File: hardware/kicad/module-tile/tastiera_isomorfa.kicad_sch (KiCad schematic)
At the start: 4 parts, among them J1 Conn_LEFT, J2 Conn_TOP, J3 Conn_BOTTOM, J4 Conn_RIGHT

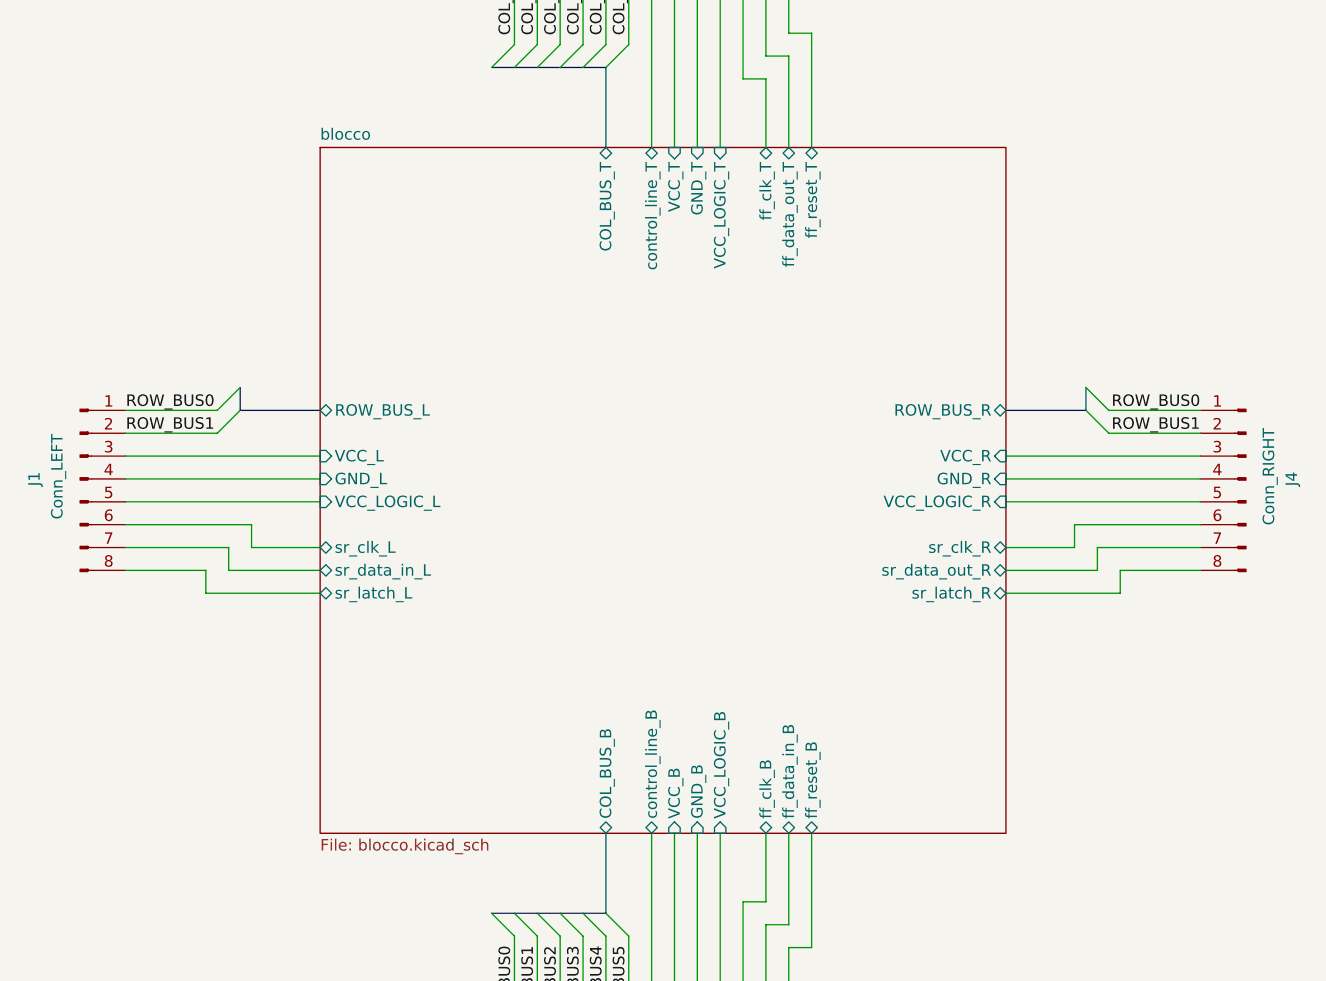
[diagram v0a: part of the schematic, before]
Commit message: Added horizontal control line UTF-8 like. Updated capacitor and resistor values.
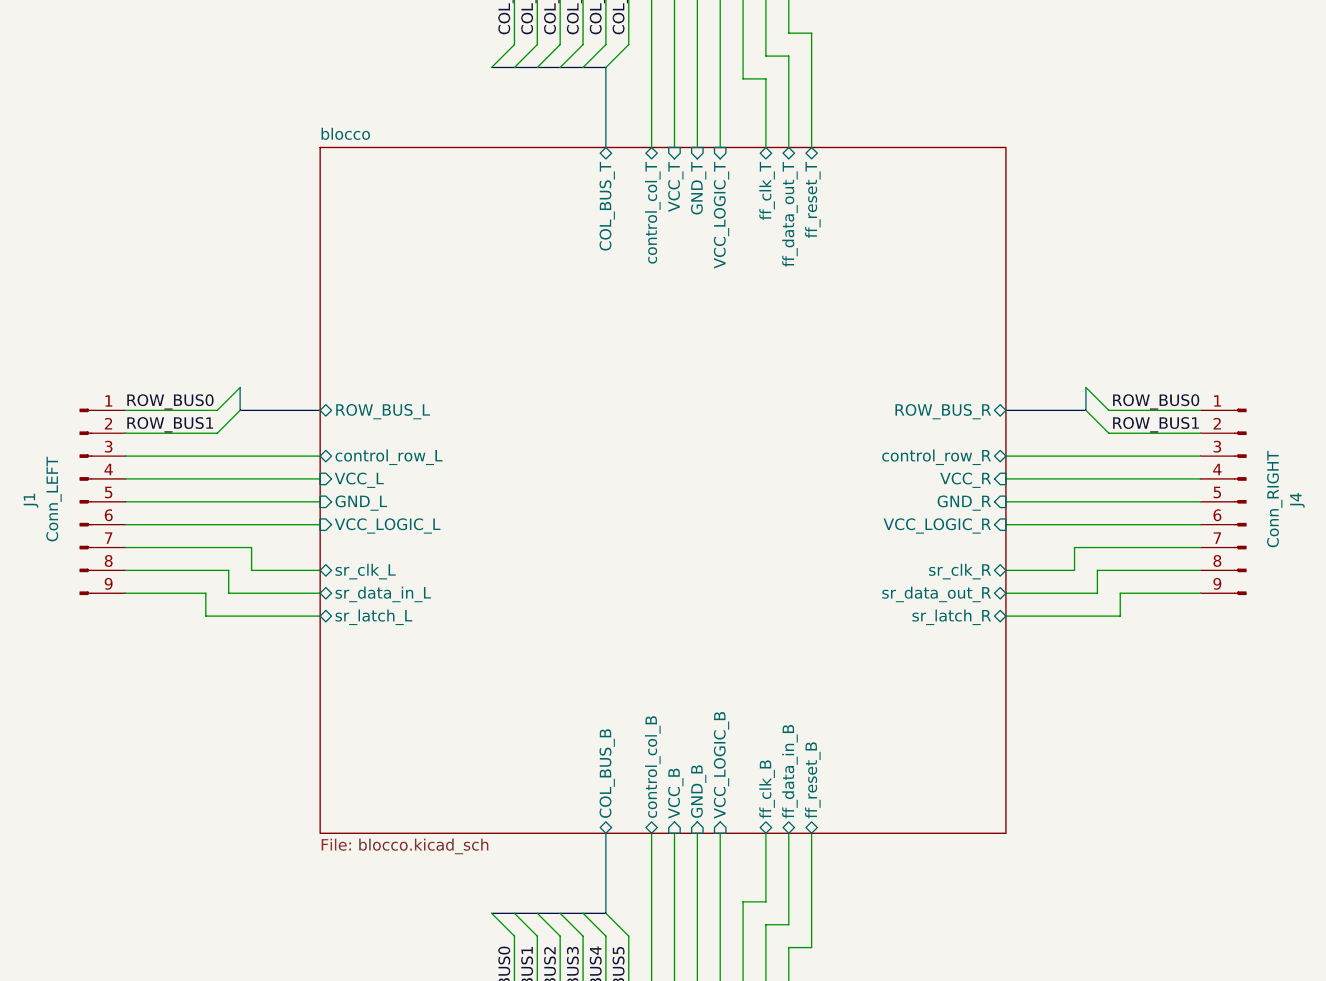
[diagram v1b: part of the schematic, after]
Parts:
- removed J1: Conn_LEFT, symbol Connector:Conn_01x08_Pin
- removed J4: Conn_RIGHT, symbol Connector:Conn_01x08_Pin
- added J1: Conn_LEFT, symbol Connector:Conn_01x09_Pin
- added J4: Conn_RIGHT, symbol Connector:Conn_01x09_Pin
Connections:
- net ROW_BUS0: now also J1.1 (Pin_1), J4.1 (Pin_1)
- net ROW_BUS1: now also J1.2 (Pin_2), J4.2 (Pin_2)
- net blocco/GND_L: now also J1.5 (Pin_5)
- net blocco/GND_R: now also J4.5 (Pin_5)
- net blocco/VCC_L: now also J1.4 (Pin_4)
- net blocco/VCC_LOGIC_L: now also J1.6 (Pin_6)
- net blocco/VCC_LOGIC_R: now also J4.6 (Pin_6)
- net blocco/VCC_R: now also J4.4 (Pin_4)
- net blocco/sr_clk_L: now also J1.7 (Pin_7)
- net blocco/sr_clk_R: now also J4.7 (Pin_7)
- net blocco/sr_data_in_L: now also J1.8 (Pin_8)
- net blocco/sr_data_out_R: now also J4.8 (Pin_8)
- net blocco/sr_latch_L: now also J1.9 (Pin_9)
- net blocco/sr_latch_R: now also J4.9 (Pin_9)
- net blocco/control_line_B renamed blocco/control_col_B
- net blocco/control_line_T renamed blocco/control_col_T
- new net blocco/control_row_L: J1.3 (Pin_3)
- new net blocco/control_row_R: J4.3 (Pin_3)
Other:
- sheet blocco ports: added control_col_B, control_col_T, control_row_L, control_row_R; removed control_line_B, control_line_T

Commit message: starting new topology
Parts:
- removed J1: Conn_LEFT, symbol Connector:Conn_01x09_Pin
- removed J2: Conn_TOP, symbol Connector:Conn_01x13_Pin
- removed J3: Conn_BOTTOM, symbol Connector:Conn_01x13_Pin
- removed J4: Conn_RIGHT, symbol Connector:Conn_01x09_Pin
- added SW1, SW10, SW11, SW12, SW2, SW3, SW4, SW5, SW6, SW7, SW8, SW9: ~, symbol Switch:SW_Push_45deg
- added U1, U2: 74HC165, symbol 74xx:74HC165
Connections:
- new net: SW1.1, SW10.1, SW11.1, SW12.1, SW2.1, SW3.1, SW4.1, SW5.1, SW6.1, SW7.1, SW8.1, SW9.1
- new net: SW12.2, U1.6 (D7)
- new net: SW8.2, U1.14 (D3)
- new net: U1.10 (DS), U2.9 (Q7)
- new net: SW5.2, U1.11 (D0)
- new net: SW6.2, U1.12 (D1)
- new net: SW7.2, U1.13 (D2)
- new net: SW9.2, U1.3 (D4)
- new net: SW10.2, U1.4 (D5)
- new net: SW11.2, U1.5 (D6)
- new net: SW4.2, U2.6 (D7)
- new net: SW2.2, U2.4 (D5)
- new net: SW1.2, U2.3 (D4)
- new net: SW3.2, U2.5 (D6)
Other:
- removed sheet blocco

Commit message: Init VHDL simulation
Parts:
- added R1, R2, R3: R, symbol Device:R
- added U3, U4: 74AHCT125, symbol 74xx:74AHCT125
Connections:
- net at SW1.1, SW10.1, SW11.1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: now also R3.1
- net at U2.10 (DS): now also U3.8, U4.8
- net at U2.11 (D0): now also R2.2
- net at U2.12 (D1): now also R1.2
- new net: U3.5, U4.5
- new net: U3.2, U4.2
- new net VCC: R1.1, R2.1, R3.2

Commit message: Start kicad design
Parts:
- removed R1, R2, R3: R, symbol Device:R
- removed SW1, SW10, SW11, SW12, SW2, SW3, SW4, SW5, SW6, SW7, SW8, SW9: ~, symbol Switch:SW_Push_45deg
- removed U3, U4: 74AHCT125, symbol 74xx:74AHCT125
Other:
- added sheet keyboard (keyboard.kicad_sch)

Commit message: Improving schematics
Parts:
- added U4: 74AUC2G08, symbol 74xGxx:74AUC2G08
- added U5: 74LS73, symbol 74xx:74LS73
- added U6: 74AUC2G125, symbol 74xGxx:74AUC2G125
- added U7: 74AUC2G126, symbol 74xGxx:74AUC2G126
- added U8: 74AHC1G32, symbol 74xGxx:74AHC1G32
- added U9: 74AHC1G04, symbol 74xGxx:74AHC1G04
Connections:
- net counter/~{rst}: now reaches U1.1 (~{PL})
- net counter/~{rst}: now also U2.1 (~{PL}), U9.4
- net BTNs7: now reaches U1.11 (D0)
- net BTNs6: now reaches U1.12 (D1)
- net BTNs5: now reaches U1.13 (D2)
- net BTNs4: now reaches U1.14 (D3)
- net GND: now reaches U1.15 (~{CE})
- net GND: now also U1.8 (GND), U2.15 (~{CE}), U2.8 (GND), U8.3 (GND), U9.3 (GND)
- net VCC: now reaches U1.16 (VCC)
- net VCC: now also U2.13 (D2), U2.14 (D3), U2.16 (VCC), U8.5 (VCC), U9.5 (VCC)
- net B_clk: now reaches U1.2 (CP)
- net B_clk: now also U2.2 (CP), U6.2, U7.2
- net BTNs3: now reaches U1.3 (D4)
- net BTNs2: now reaches U1.4 (D5)
- net BTNs1: now reaches U1.5 (D6)
- net BTNs0: now reaches U1.6 (D7)
- net B_data: now reaches U1.9 (Q7)
- net at U2.10 (DS): now also U6.3, U7.3
- net T_endcol: now reaches U2.11 (D0)
- net L_endrow: now reaches U2.12 (D1)
- net BTNs11: now reaches U2.3 (D4)
- net BTNs10: now reaches U2.4 (D5)
- net BTNs9: now reaches U2.5 (D6)
- net BTNs8: now reaches U2.6 (D7)
- new net: U4.3, U6.1, U6.7, U7.1, U7.7
- new net B_first: U4.6
- new net B_latch: U8.1
- new net L_clk: U7.6
- new net L_data: U7.5
- new net L_latch: U8.4, U9.2
- new net R_latch: U8.2
- new net T_W: U4.5
- new net T_clk: U6.6
- no-connect marks 0 -> 2
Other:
- added sheet counter (counter.kicad_sch)
- sheet keyboard ports: added BTNs; removed none
- moved on the sheet: U1, U2

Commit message: Schematics update
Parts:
- removed U1, U2: 74HC165, symbol 74xx:74HC165
- removed U4: 74AUC2G08, symbol 74xGxx:74AUC2G08
- removed U5: 74LS73, symbol 74xx:74LS73
- removed U6: 74AUC2G125, symbol 74xGxx:74AUC2G125
- removed U7: 74AUC2G126, symbol 74xGxx:74AUC2G126
- removed U8: 74AHC1G32, symbol 74xGxx:74AHC1G32
- removed U9: 74AHC1G04, symbol 74xGxx:74AHC1G04
- added J1, J2: Conn_01x08, symbol Connector_Generic:Conn_01x08
- added J3, J4: Conn_01x06, symbol Connector_Generic:Conn_01x06
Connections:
- net GND: now also J1.8 (Pin_8), J2.8 (Pin_8), J3.6 (Pin_6), J4.6 (Pin_6)
- net VCC: now also J1.1 (Pin_1), J2.1 (Pin_1), J3.1 (Pin_1), J4.1 (Pin_1)
- new net tile/B_W: J1.7 (Pin_7)
- new net tile/B_clk: J1.2 (Pin_2)
- new net tile/B_data: J1.3 (Pin_3)
- new net tile/B_endcol: J1.4 (Pin_4)
- new net tile/B_first: J1.5 (Pin_5)
- new net tile/B_latch: J1.6 (Pin_6)
- new net tile/L_clk: J3.2 (Pin_2)
- new net tile/L_data: J3.3 (Pin_3)
- new net tile/L_endrow: J3.4 (Pin_4)
- new net tile/L_latch: J3.5 (Pin_5)
- new net tile/R_clk: J4.2 (Pin_2)
- new net tile/R_data: J4.3 (Pin_3)
- new net tile/R_endrow: J4.4 (Pin_4)
- new net tile/R_latch: J4.5 (Pin_5)
- new net tile/T_W: J2.7 (Pin_7)
- new net tile/T_clk: J2.2 (Pin_2)
- new net tile/T_data: J2.3 (Pin_3)
- new net tile/T_endcol: J2.4 (Pin_4)
- new net tile/T_first: J2.5 (Pin_5)
- new net tile/T_latch: J2.6 (Pin_6)
- no-connect marks 2 -> 0
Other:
- removed sheet counter
- removed sheet keyboard
- added sheet tile (tile.kicad_sch)

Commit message: Schematic complete
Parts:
- J101: renamed from J3; value Conn_01x06 -> Conn_LEFT; footprint (none) -> Connector_PinHeader_2.54mm:PinHeader_1x06_P2.54mm_Vertical
- J102: renamed from J2; value Conn_01x08 -> Conn_TOP; footprint (none) -> Connector_PinHeader_2.54mm:PinHeader_1x08_P2.54mm_Vertical
- J103: renamed from J1; value Conn_01x08 -> Conn_BOTTOM; footprint (none) -> Connector_PinHeader_2.54mm:PinHeader_1x08_P2.54mm_Vertical
- J104: renamed from J4; value Conn_01x06 -> Conn_RIGHT; footprint (none) -> Connector_PinHeader_2.54mm:PinHeader_1x06_P2.54mm_Vertical
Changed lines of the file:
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@@
 		(on_board yes)
 		(dnp no)
-		(property "Reference" "J2"
+		(property "Reference" "J102"
 			(at 152.4 40.64 90)
 			(effects
@@
 			)
 		)
-		(property "Value" "Conn_01x08"
+		(property "Value" "Conn_TOP"
 			(at 152.4 38.1 90)
 			(effects
@@
 			)
 		)
-		(property "Footprint" ""
+		(property "Footprint" "Connector_PinHeader_2.54mm:PinHeader_1x08_P2.54mm_Vertical"
 			(at 151.13 44.45 0)
 			(effects
@@
 			)
 		)
+		(property "Codice" ""
+			(at 151.13 44.45 90)
+			(effects
+				(font
+					(size 1.27 1.27)
+				)
+				(hide yes)
+			)
+		)
+		(property "Link" ""
+			(at 151.13 44.45 90)
+			(effects
+				(font
+					(size 1.27 1.27)
+				)
+				(hide yes)
+			)
+		)
 		(pin "7"
 		)
@@
 			(project "tastiera_isomorfa"
 				(path "/2a6329ec-b0e8-4012-8f5a-476608b8b2cc"
-					(reference "J2")
+					(reference "J102")
 					(unit 1)
 				)
@@
 		(dnp no)
 		(fields_autoplaced yes)
-		(property "Reference" "#PWR029"
+		(property "Reference" "#PWR0103"
 			(at 137.16 53.34 0)
 			(effects
@@
 			(project ""
 				(path "/2a6329ec-b0e8-4012-8f5a-476608b8b2cc"
-					(reference "#PWR029")
+					(reference "#PWR0103")
 					(unit 1)
 				)
@@
 		(dnp no)
 		(fields_autoplaced yes)
-		(property "Reference" "J3"
+		(property "Reference" "J101"
 			(at 100.33 83.82 0)
 			(effects
@@
 			)
 		)
-		(property "Value" "Conn_01x06"
+		(property "Value" "Conn_LEFT"
 			(at 100.33 86.36 0)
 			(effects
@@
 			)
 		)
-		(property "Footprint" ""
+		(property "Footprint" "Connector_PinHeader_2.54mm:PinHeader_1x06_P2.54mm_Vertical"
 			(at 100.33 95.25 0)
 			(effects
@@
 			)
 		)
+		(property "Codice" ""
+			(at 100.33 95.25 0)
+			(effects
+				(font
+					(size 1.27 1.27)
+				)
+				(hide yes)
+			)
+		)
+		(property "Link" ""
+			(at 100.33 95.25 0)
+			(effects
+				(font
+					(size 1.27 1.27)
+				)
+				(hide yes)
+			)
+		)
 		(pin "1"
 		)
@@
 			(project ""
 				(path "/2a6329ec-b0e8-4012-8f5a-476608b8b2cc"
-					(reference "J3")
+					(reference "J101")
 					(unit 1)
 				)
@@
 		(dnp no)
 		(fields_autoplaced yes)
-		(property "Reference" "#PWR036"
+		(property "Reference" "#PWR0102"
 			(at 109.22 113.03 0)
 			(effects
@@
 			(project ""
 				(path "/2a6329ec-b0e8-4012-8f5a-476608b8b2cc"
-					(reference "#PWR036")
+					(reference "#PWR0102")
 					(unit 1)
 				)
@@
 		(dnp no)
 		(fields_autoplaced yes)
-		(property "Reference" "#PWR035"
+		(property "Reference" "#PWR0108"
 			(at 195.58 113.03 0)
 			(effects
@@
 			(project ""
 				(path "/2a6329ec-b0e8-4012-8f5a-476608b8b2cc"
-					(reference "#PWR035")
+					(reference "#PWR0108")
 					(unit 1)
 				)
@@
 		(dnp no)
 		(fields_autoplaced yes)
-		(property "Reference" "#PWR034"
+		(property "Reference" "#PWR0106"
 			(at 167.64 149.86 0)
 			(effects
@@
 			(project ""
 				(path "/2a6329ec-b0e8-4012-8f5a-476608b8b2cc"
-					(reference "#PWR034")
+					(reference "#PWR0106")
 					(unit 1)
 				)
@@
 		(dnp no)
 		(fields_autoplaced yes)
-		(property "Reference" "#PWR030"
+		(property "Reference" "#PWR0104"
 			(at 143.51 147.32 0)
 			(effects
@@
 			(project ""
 				(path "/2a6329ec-b0e8-4012-8f5a-476608b8b2cc"
-					(reference "#PWR030")
+					(reference "#PWR0104")
 					(unit 1)
 				)
@@
 		(dnp no)
 		(fields_autoplaced yes)
-		(property "Reference" "#PWR031"
+		(property "Reference" "#PWR0107"
 			(at 195.58 91.44 0)
 			(effects
@@
 			(project ""
 				(path "/2a6329ec-b0e8-4012-8f5a-476608b8b2cc"
-					(reference "#PWR031")
+					(reference "#PWR0107")
 					(unit 1)
 				)
@@
 		(dnp no)
 		(fields_autoplaced yes)
-		(property "Reference" "#PWR033"
+		(property "Reference" "#PWR0105"
 			(at 161.29 55.88 0)
 			(effects
@@
 			(project ""
 				(path "/2a6329ec-b0e8-4012-8f5a-476608b8b2cc"
-					(reference "#PWR033")
+					(reference "#PWR0105")
 					(unit 1)
 				)
@@
 		(dnp no)
 		(fields_autoplaced yes)
-		(property "Reference" "#PWR032"
+		(property "Reference" "#PWR0101"
 			(at 109.22 91.44 0)
 			(effects
@@
 			(project ""
 				(path "/2a6329ec-b0e8-4012-8f5a-476608b8b2cc"
-					(reference "#PWR032")
+					(reference "#PWR0101")
 					(unit 1)
 				)
@@
 		(dnp no)
 		(fields_autoplaced yes)
-		(property "Reference" "J4"
-			(at 204.47 83.82 0)
-			(effects
-				(font
-					(size 1.27 1.27)
-				)
-			)
-		)
-		(property "Value" "Conn_01x06"
-			(at 204.47 86.36 0)
-			(effects
-				(font
-					(size 1.27 1.27)
-				)
-			)
-		)
-		(property "Footprint" ""
+		(property "Reference" "J104"
+			(at 207.01 95.2499 0)
+			(effects
+				(font
+					(size 1.27 1.27)
+				)
+				(justify left)
+			)
+		)
+		(property "Value" "Conn_RIGHT"
+			(at 207.01 97.7899 0)
+			(effects
+				(font
+					(size 1.27 1.27)
+				)
+				(justify left)
+			)
+		)
+		(property "Footprint" "Connector_PinHeader_2.54mm:PinHeader_1x06_P2.54mm_Vertical"
 			(at 204.47 95.25 0)
 			(effects
@@
 			)
 		)
+		(property "Codice" ""
+			(at 204.47 95.25 0)
+			(effects
+				(font
+					(size 1.27 1.27)
+				)
+				(hide yes)
+			)
+		)
+		(property "Link" ""
+			(at 204.47 95.25 0)
+			(effects
+				(font
+					(size 1.27 1.27)
+				)
+				(hide yes)
+			)
+		)
 		(pin "1"
 		)
@@
 			(project "tastiera_isomorfa"
 				(path "/2a6329ec-b0e8-4012-8f5a-476608b8b2cc"
-					(reference "J4")
+					(reference "J104")
 					(unit 1)
 				)
@@
 		(on_board yes)
 		(dnp no)
-		(property "Reference" "J1"
+		(property "Reference" "J103"
 			(at 152.4 152.4 90)
 			(effects
@@
 			)
 		)
-		(property "Value" "Conn_01x08"
+		(property "Value" "Conn_BOTTOM"
 			(at 152.4 154.94 90)
 			(effects
@@
 			)
 		)
-		(property "Footprint" ""
+		(property "Footprint" "Connector_PinHeader_2.54mm:PinHeader_1x08_P2.54mm_Vertical"
 			(at 151.13 148.59 0)
 			(effects
@@
 			)
 		)
+		(property "Codice" ""
+			(at 151.13 148.59 90)
+			(effects
+				(font
+					(size 1.27 1.27)
+				)
+				(hide yes)
+			)
+		)
+		(property "Link" ""
+			(at 151.13 148.59 90)
+			(effects
+				(font
+					(size 1.27 1.27)
+				)
+				(hide yes)
+			)
+		)
 		(pin "7"
 		)
@@
 			(project ""
 				(path "/2a6329ec-b0e8-4012-8f5a-476608b8b2cc"
-					(reference "J1")
-					(unit 1)
-				)
+					(reference "J103")
+					(unit 1)
+				)

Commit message: First commit new branch
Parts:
- added J105: BTNs_L_MSB, Connector_PinSocket_2.54mm:PinSocket_1x08_P2.54mm_Vertical, symbol Connector_Generic:Conn_01x08
- added J106: BTNs_L_LSB, Connector_PinSocket_2.54mm:PinSocket_1x08_P2.54mm_Vertical, symbol Connector_Generic:Conn_01x08
- added J107: BTNs_MSB, Connector_PinHeader_2.54mm:PinHeader_1x08_P2.54mm_Vertical, symbol Connector_Generic:Conn_01x08
- added J108: BTNs_LSB, Connector_PinHeader_2.54mm:PinHeader_1x08_P2.54mm_Vertical, symbol Connector_Generic:Conn_01x08
- J101: footprint Connector_PinHeader_2.54mm:PinHeader_1x06_P2.54mm_Vertical -> Connector_PinSocket_2.54mm:PinSocket_1x06_P2.54mm_Horizontal
- J102: footprint Connector_PinHeader_2.54mm:PinHeader_1x08_P2.54mm_Vertical -> Connector_PinSocket_2.54mm:PinSocket_1x08_P2.54mm_Horizontal
- J103: footprint Connector_PinHeader_2.54mm:PinHeader_1x08_P2.54mm_Vertical -> Connector_PinHeader_2.54mm:PinHeader_1x08_P2.54mm_Horizontal
- J104: footprint Connector_PinHeader_2.54mm:PinHeader_1x06_P2.54mm_Vertical -> Connector_PinHeader_2.54mm:PinHeader_1x06_P2.54mm_Horizontal
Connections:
- net GND: now also J105.8 (Pin_8), J106.8 (Pin_8)
- net VCC: now also J105.1 (Pin_1), J106.1 (Pin_1)
- new net BTNs0: J108.2 (Pin_2)
- new net BTNs1: J108.3 (Pin_3)
- new net BTNs10: J107.6 (Pin_6)
- new net BTNs11: J107.7 (Pin_7)
- new net BTNs2: J108.4 (Pin_4)
- new net BTNs3: J108.5 (Pin_5)
- new net BTNs4: J108.6 (Pin_6)
- new net BTNs5: J108.7 (Pin_7)
- new net BTNs6: J107.2 (Pin_2)
- new net BTNs7: J107.3 (Pin_3)
- new net BTNs8: J107.4 (Pin_4)
- new net BTNs9: J107.5 (Pin_5)
- new net BTNs_L0: J106.2 (Pin_2)
- new net BTNs_L1: J106.3 (Pin_3)
- new net BTNs_L10: J105.6 (Pin_6)
- new net BTNs_L11: J105.7 (Pin_7)
- new net BTNs_L2: J106.4 (Pin_4)
- new net BTNs_L3: J106.5 (Pin_5)
- new net BTNs_L4: J106.6 (Pin_6)
- new net BTNs_L5: J106.7 (Pin_7)
- new net BTNs_L6: J105.2 (Pin_2)
- new net BTNs_L7: J105.3 (Pin_3)
- new net BTNs_L8: J105.4 (Pin_4)
- new net BTNs_L9: J105.5 (Pin_5)
- new net GND_T: J107.8 (Pin_8), J108.8 (Pin_8)
- new net VCC_T: J107.1 (Pin_1), J108.1 (Pin_1)
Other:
- added sheet keyboard (keyboard.kicad_sch)
- sheet tile ports: added BTNs_L[0..11]; removed none
- moved on the sheet: J101, J102, J103, J104
